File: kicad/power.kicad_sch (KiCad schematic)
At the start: 44 parts, among them U1 NE5532, U2 NE5532, U3 NE5532, U4 NE5532, U5 NE5532, U6 NE5532

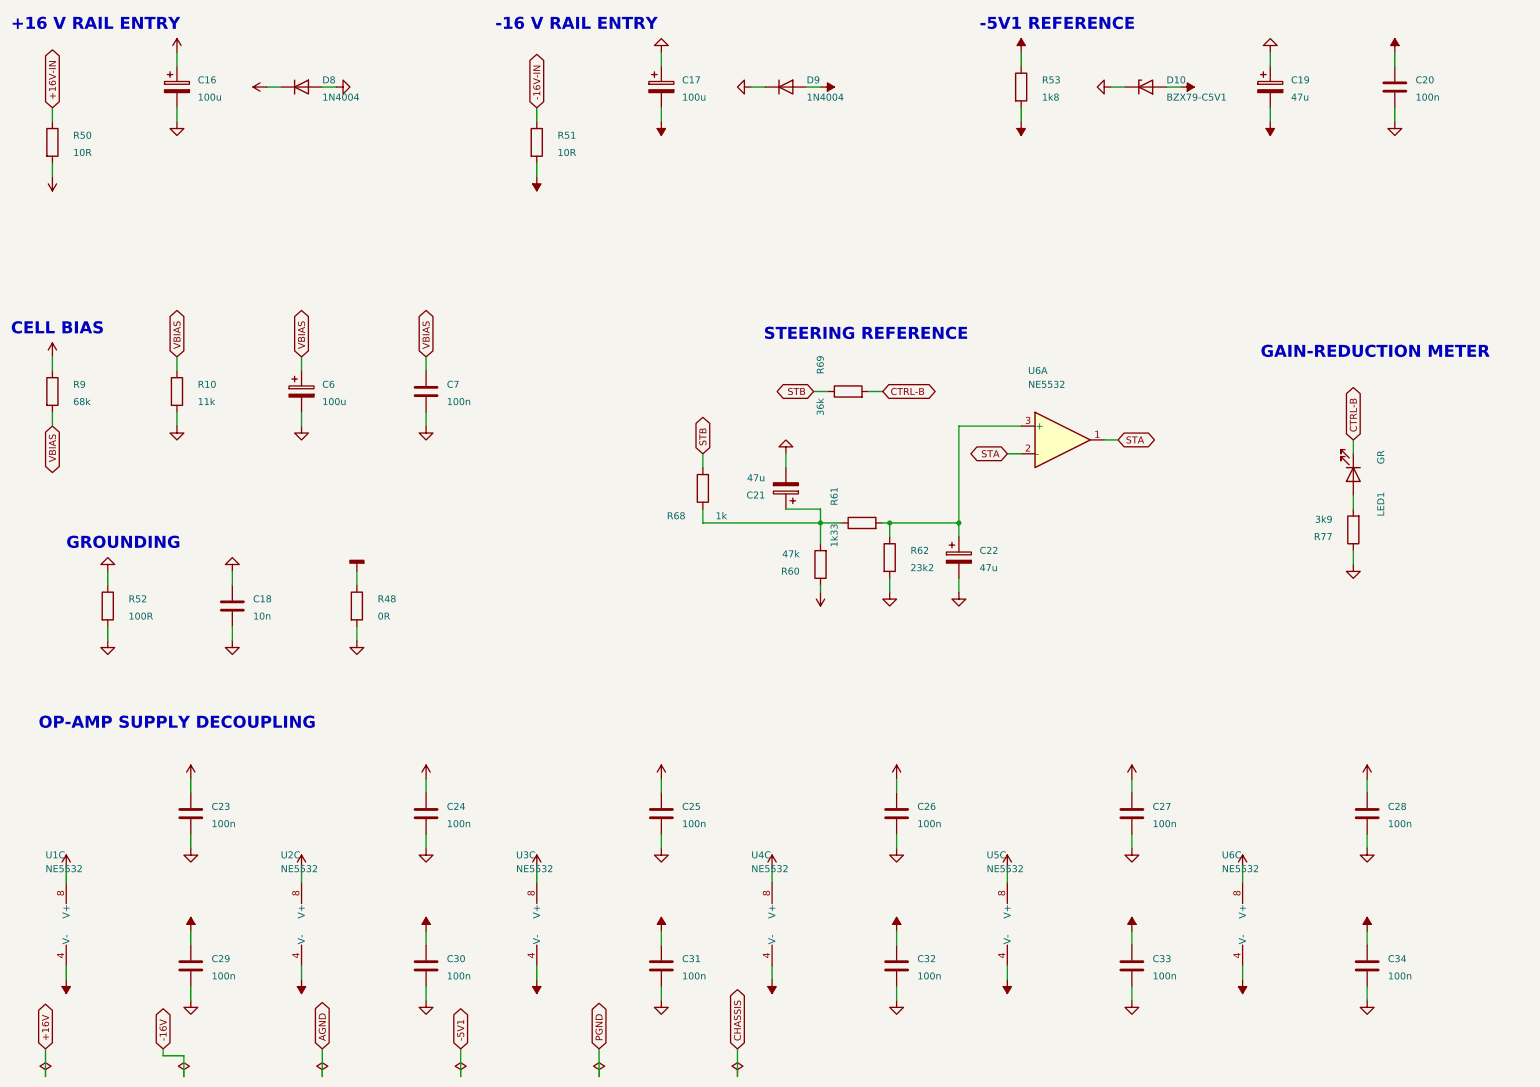
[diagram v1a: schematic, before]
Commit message: Add reorganised schematic to split files.
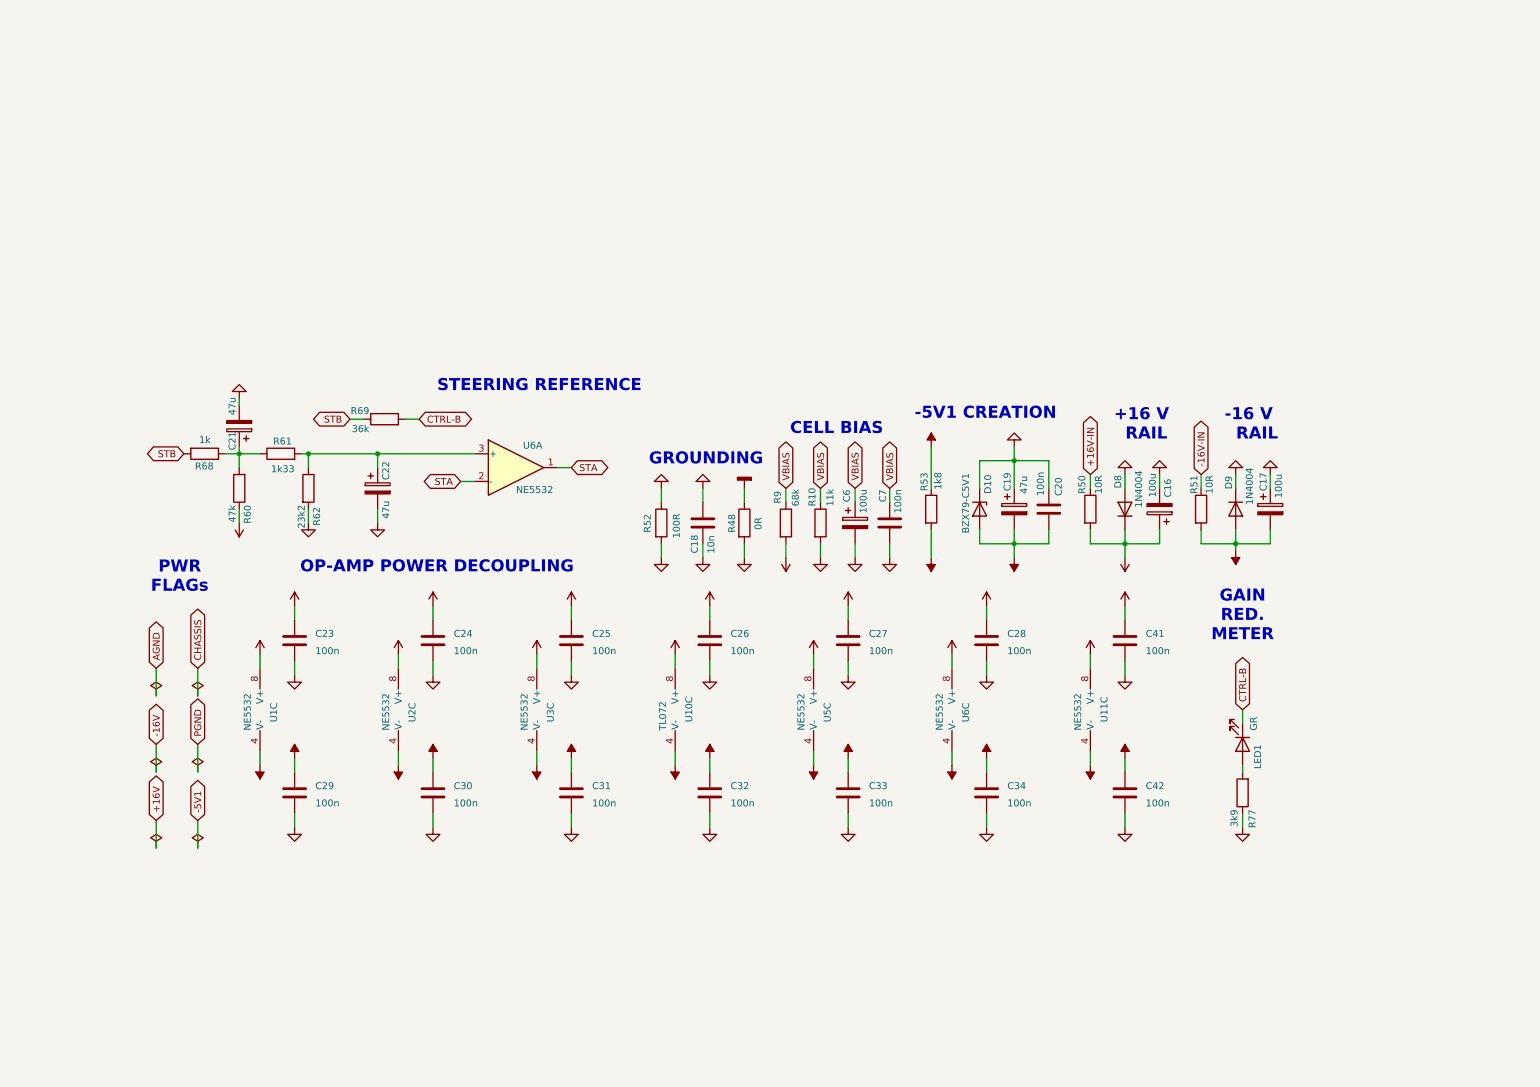
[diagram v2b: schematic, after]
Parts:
- removed U4: NE5532, Package_DIP:DIP-8_W7.62mm, symbol Amplifier_Operational:NE5532
- added C41, C42: 100n, Capacitor_THT:C_Disc_D5.0mm_W2.5mm_P5.00mm, symbol Device:C
- added U10: TL072, Package_DIP:DIP-8_W7.62mm_Socket, symbol Amplifier_Operational:NE5532
- added U11: NE5532, Package_DIP:DIP-8_W7.62mm_Socket, symbol Amplifier_Operational:NE5532
- U1, U2, U3, U5, U6: footprint Package_DIP:DIP-8_W7.62mm -> Package_DIP:DIP-8_W7.62mm_Socket
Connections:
- net +16V: now also R9.2, C41.1, U10.8 (V+), U11.8 (V+); no longer R9.1
- net -16V: now also C42.1, U10.4 (V-), U11.4 (V-)
- net AGND: now also C41.2, C42.2
- net VBIAS: now also R9.1; no longer R9.2
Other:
- note added: "+16 V RAIL"
- note added: "-16 V RAIL"
- note added: "-5V1 CREATION"
- note added: "GAIN RED. METER"
- note added: "OP-AMP POWER DECOUPLING"
- note added: "PWR FLAGs"
- note removed: "+16 V RAIL ENTRY"
- note removed: "-16 V RAIL ENTRY"
- note removed: "-5V1 REFERENCE"
- note removed: "GAIN-REDUCTION METER"
- note removed: "OP-AMP SUPPLY DECOUPLING"

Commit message: Match the split sheets' chip references to the board (#4)
Pasting the board schematic into the split sheets renumbered five units:
the VCA recovery amp was U4B (board U1B), the sidechain TL072 was U10
(board U4), U4's power unit was U10, U7's power unit was U11, and the
LM3915 was U12 (board U10). They now carry the board's references, so
the split sheets and compressor_with_pcb have the same 167 parts and the
same 119 nets.
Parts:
- renumbered U10 to U4, U11 to U7
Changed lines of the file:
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@@
 		(in_pos_files yes)
 		(dnp no)
-		(property "Reference" "U11"
+		(property "Reference" "U7"
 			(at 224.79 149.606 90)
 			(show_name no)
@@
 			(project "UTS Mini Mixing Desk - Compressor"
 				(path "/fdeae63a-37f5-58fb-b342-cb68d8a6bfbc/c5adaca6-1d0e-5bdd-9154-62aca7332af4"
-					(reference "U11")
+					(reference "U7")
 					(unit 3)
 				)
@@
 		(in_pos_files yes)
 		(dnp no)
-		(property "Reference" "U10"
+		(property "Reference" "U4"
 			(at 148.59 149.606 90)
 			(show_name no)
@@
 			(project "UTS Mini Mixing Desk - Compressor"
 				(path "/fdeae63a-37f5-58fb-b342-cb68d8a6bfbc/c5adaca6-1d0e-5bdd-9154-62aca7332af4"
-					(reference "U10")
+					(reference "U4")
 					(unit 3)
 				)

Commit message: Simulate the compressor, fix its values, and fit Altronics parts (#5)
* Make the schematic simulate in KiCad, and add the simulation results

Every part on the kicad/ sheets now has a SPICE model (Sim.* fields, models in
kicad/sim/compressor_models.lib), the connectors are excluded from simulation, and the
root sheet carries a test bench: the rack's supplies, a balanced source, a load and the
knob settings as .param lines. The netlist is unchanged.

tools/add_sim_models.py writes the fields. tools/sim/run_all.py exports the netlist with
kicad-cli and runs the characterisation in ngspice; kicad/sim/README.md has how to run
it in KiCad and what it found.

* Bring the compressor's values in line with the design targets

Through gain: R21/R22 3k3 to 6k8 halves the recovery amp's gain, so the
module is unity balanced in to out and BYPASS matches; R36 100k to 200k
keeps the detector's level. Bass: C9/C10 2u2 to 4u7 with the larger
input resistors puts the -3 dB point near 5 Hz.
Threshold: RV3 1M linear to 250k audio taper and R35 20k to 2k4 spread
about -20 to +20 dBu over the knob. R60 47k to 24k sets the resting
steer near 150 mV.
Timing: R45/R46/RV5 and R47/RV6/R74 scaled up to match the RC targets
with the same C15.

Same changes on the sheets, both boards and design.py. The simulation's
pot model gains an audio taper, and the burst test now runs at half
threshold.

* Carry the new values onto both boards' schematics and layouts

* Retune attack and release: R45 220R, R46 47R, RV5 10k, R47 15k

The first pass ran the attack too slow (9 to 103 ms against a 2.7 to
50 ms target). Results are regenerated in the next commit.

* Regenerate the simulation results for the new values

* Stop the fast-attack overshoot: C22 47u to 4u7

C22 made STA lag STB by about 60 ms, so when CTRL-B pulled the
reference node down the steering kept moving after the control
voltage had settled, overshooting by up to 20 dB. With 4u7 the two
sides track and the overshoot is about 1 dB. RV5 back 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
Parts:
- C22: value 47u -> 4u7
- R60: value 47k -> 24k
